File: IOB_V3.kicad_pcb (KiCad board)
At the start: 2 copper layers, 290 parts, among them J1 Conn_01x02, J10 Conn_01x04, J11 Conn_01x04, J12 Conn_01x04, J13 Conn_01x04, J14 Conn_01x04, J15 Conn_01x08, J16 Conn_02x04_Odd_Even, J17 Conn_01x04_MountingPin, J18 Conn_01x04_MountingPin, J19 Conn_01x04_MountingPin, J2 Conn_01x03, J20 Conn_01x04_MountingPin, J21 Conn_01x04_MountingPin, J22 Conn_01x04_MountingPin, J23 Conn_01x04_MountingPin, J24 Conn_01x04_MountingPin, J3 Conn_01x04, J4 Conn_01x04, J5 Conn_01x04, J6 Conn_01x04, J7 Conn_01x04, J8 Conn_01x04, J9 Conn_01x04, Q1 BSZ0902NSATMA1, Q10 BSZ0902NSATMA1, Q11 BSZ0902NSATMA1, Q12 BSZ0902NSATMA1, Q2 BSZ0902NSATMA1, Q3 BSZ0902NSATMA1, Q4 BSZ0902NSATMA1, Q5 BSZ0902NSATMA1, Q6 BSZ0902NSATMA1, Q7 BSZ0902NSATMA1, Q8 BSZ0902NSATMA1, Q9 BSZ0902NSATMA1, SW1 SW_Push_Dual, SW2 SW_Push_Dual, SW3 SW_DIP_x08, U1 REF3033, U10 INA180, U11 INA180, U12 INA180, U13 INA180, U14 TS30041, U15 MCP1700-3302E_SOT23, U16 MCP2562FD, U17 MCP2562FD, U18 STM32G474MET3, U19 W25Q256JV, U2 INA180, U3 INA180, U4 INA180, U5 INA180, U6 INA180, U7 INA180, U8 INA180, U9 INA180, X1 TXC-7C

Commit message: WIP
for @Markus
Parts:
- removed J20, J21, J22, J23, J24: Conn_01x04_MountingPin, Connector_JST:JST_GH_BM04B-GHS-TBT_1x04-1MP_P1.25mm_Vertical
- removed JP10, JP15, JP16, JP21, JP22, JP27, JP28, JP3, JP33, JP34, JP39, JP4, JP40, JP45, JP46, JP51, JP52, JP57, JP58, JP63, JP64, JP69, JP70, JP9: Jumper_2_Open, Jumper:SolderJumper-2_P1.3mm_Open_TrianglePad1.0x1.5mm
- removed R91: 120R, Resistor_SMD:R_0603_1608Metric
- added C23: 1u, Capacitor_SMD:C_0603_1608Metric, F.Cu at (137.5, 104.1)
- added R93: 0R, Resistor_SMD:R_0603_1608Metric, F.Cu at (134.5, 35.1)
- added R94: Rpullup, Resistor_SMD:R_0603_1608Metric, F.Cu at (134.5, 37.7)
- added TP2: TestPoint, TestPoint:TestPoint_THTPad_D1.0mm_Drill0.5mm, F.Cu at (138.0, 35.4)
- C11: value NP -> 100n; footprint Capacitor_SMD:CP_Elec_6.3x4.9 -> Capacitor_SMD:C_0402_1005Metric
- C12, C16, C17, C18: footprint Capacitor_SMD:C_0402_1005Metric -> Capacitor_SMD:C_0603_1608Metric
- C14: value 100n -> NP; footprint Capacitor_SMD:C_0402_1005Metric -> Capacitor_SMD:CP_Elec_6.3x4.9
- C19: value 100n -> 4.7u; footprint Capacitor_SMD:C_0402_1005Metric -> Capacitor_SMD:C_0603_1608Metric
- C20: value 100n -> 10n; footprint Capacitor_SMD:C_0402_1005Metric -> Capacitor_SMD:C_0603_1608Metric
- C21: value 10u -> 1u
- C22, C9: value 10u -> 100n
- C8: value 100n -> 10u; footprint Capacitor_SMD:C_0402_1005Metric -> Capacitor_SMD:C_0603_1608Metric
- J18: value Conn_01x04_MountingPin -> Conn_01x08; footprint Connector_JST:JST_GH_BM04B-GHS-TBT_1x04-1MP_P1.25mm_Vertical -> Connector_IDC:IDC-Header_2x04_P2.54mm_Horizontal
- U18: value STM32G474MET3 -> W25Q256JV; footprint STM32G747ME:STM32G474MET3 -> TXV_Library_Footprints:WSON-8-8x6mm
- U19: value W25Q256JV -> STM32G474MET6; footprint TXV_Library_Footprints:WSON-8-8x6mm -> STM32:STM32G474MET3
- moved J18 13.2 mm to (78.7, 33.3)
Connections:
- net /MCU/DIP_0 renamed Net-(SW3-Pad16)
- net /MCU/DIP_1 renamed Net-(SW3-Pad15)
- net /MCU/DIP_2 renamed Net-(SW3-Pad14)
- net /MCU/DIP_3 renamed Net-(SW3-Pad13)
- net /MCU/DIP_4 renamed Net-(SW3-Pad12)
- net /MCU/DIP_5 renamed Net-(SW3-Pad11)
- net /MCU/DIP_6 renamed Net-(SW3-Pad10)
- net /MCU/DIP_7 renamed Net-(SW3-Pad9)
- net /Pressure/Enable1 renamed /En1
- net /Pressure/Enable2 renamed /En2
- net /Pressure/Enable6 renamed /En6
- C13 pad 1: +3V3 -> GND
- C13 pad 2: GND -> +5V
- C17 pad 1: GND -> +3V3
- C17 pad 2: +5V -> GND
- C19 pad 1: GND -> +3V3
- C19 pad 2: +5V -> GND
- C20 pad 1: +3V3 -> /MCU/VDDA
- C21 pad 1: /MCU/VCAP1 -> /MCU/VDDA
- C22 pad 1: /MCU/VCAP2 -> +3.3VA
- C8 pad 1: +3V3 -> +5V
- C9 pad 1: +5V -> +3V3
- F12 pad 2: Net-(F12-Pad2) -> Net-(F11-Pad2)
- F14 pad 2: Net-(F14-Pad2) -> Net-(F13-Pad2)
- F16 pad 2: Net-(F16-Pad2) -> Net-(F15-Pad2)
- F18 pad 2: Net-(F18-Pad2) -> Net-(F17-Pad2)
- F2 pad 2: Net-(F2-Pad2) -> Net-(F1-Pad2)
- F20 pad 2: Net-(F20-Pad2) -> Net-(F19-Pad2)
- F22 pad 2: Net-(F22-Pad2) -> Net-(F21-Pad2)
- F24 pad 2: Net-(F24-Pad2) -> Net-(F23-Pad2)
- F4 pad 2: Net-(F4-Pad2) -> Net-(F3-Pad2)
- F6 pad 2: Net-(F6-Pad2) -> Net-(F5-Pad2)
- F8 pad 2: Net-(F8-Pad2) -> Net-(F7-Pad2)
- F9 pad 2: Net-(F9-Pad2) -> Net-(F10-Pad2)
- J10 pad 1: Net-(J10-Pad1) -> Net-(F15-Pad2)
- J11 pad 1: Net-(J11-Pad1) -> Net-(F17-Pad2)
- J12 pad 1: Net-(J12-Pad1) -> Net-(F19-Pad2)
- J13 pad 1: Net-(J13-Pad1) -> Net-(F21-Pad2)
- J14 pad 1: Net-(J14-Pad1) -> Net-(F23-Pad2)
- J18 pad 1: +5V -> unconnected-(J18-Pad1)
- J18 pad 2: /MCU/CANH2 -> unconnected-(J18-Pad2)
- J18 pad 3: /MCU/CANL2 -> unconnected-(J18-Pad3)
- J18 pad 4: GND -> unconnected-(J18-Pad4)
- J3 pad 1: Net-(J3-Pad1) -> Net-(F1-Pad2)
- J4 pad 1: Net-(J4-Pad1) -> Net-(F3-Pad2)
- J5 pad 1: Net-(J5-Pad1) -> Net-(F5-Pad2)
- J6 pad 1: Net-(J6-Pad1) -> Net-(F7-Pad2)
- J7 pad 1: Net-(J7-Pad1) -> Net-(F10-Pad2)
- J8 pad 1: Net-(J8-Pad1) -> Net-(F11-Pad2)
- J9 pad 1: Net-(J9-Pad1) -> Net-(F13-Pad2)
- JP11 pad 2: /Pressure/Select2 -> /Select2
- JP12 pad 1: /Pressure/Select2 -> /Select2
- JP17 pad 2: /Pressure/Select3 -> /Select3
- JP18 pad 1: /Pressure/Select3 -> /Select3
- JP23 pad 2: /Pressure/Select4 -> /Select4
- JP24 pad 1: /Pressure/Select4 -> /Select4
- JP29 pad 2: /Pressure/Select5 -> /Select5
- JP30 pad 1: /Pressure/Select5 -> /Select5
- JP35 pad 2: /Pressure/Select6 -> /Select6
- JP36 pad 1: /Pressure/Select6 -> /Select6
- JP41 pad 2: /Pressure/Select7 -> /Select7
- JP42 pad 1: /Pressure/Select7 -> /Select7
- JP47 pad 2: /Pressure/Select8 -> /Select8
- JP48 pad 1: /Pressure/Select8 -> /Select8
- JP5 pad 2: /Pressure/Select1 -> /Select1
- JP53 pad 2: /Pressure/Select9 -> /Select9
- JP54 pad 1: /Pressure/Select9 -> /Select9
- JP59 pad 2: /Pressure/Select10 -> /Select10
- JP6 pad 1: /Pressure/Select1 -> /Select1
- JP60 pad 1: /Pressure/Select10 -> /Select10
- JP65 pad 2: /Pressure/Select11 -> /Select11
- JP66 pad 1: /Pressure/Select11 -> /Select11
- JP71 pad 2: /Pressure/Select12 -> /Select12
- JP72 pad 1: /Pressure/Select12 -> /Select12
- R1 pad 2: /MCU/ADC1_INP10 -> /MCU/ADC1_IN1
- R15 pad 2: /MCU/ADC3_INP0 -> /MCU/ADC2_IN12
- R16 pad 1: /MCU/ADC3_INP0 -> /MCU/ADC2_IN12
- R18 pad 1: /Pressure/Enable3 -> /En3
- R2 pad 1: /MCU/ADC1_INP10 -> /MCU/ADC1_IN1
- R22 pad 2: /MCU/ADC3_INP1 -> /MCU/ADC1_IN5
- R23 pad 1: /MCU/ADC3_INP1 -> /MCU/ADC1_IN5
- R25 pad 1: /Pressure/Enable4 -> /En4
- R29 pad 2: /MCU/ADC1_INP4 -> /MCU/ADC1_IN4
- R30 pad 1: /MCU/ADC1_INP4 -> /MCU/ADC1_IN4
- R32 pad 1: /Pressure/Enable5 -> /En5
- R36 pad 2: /MCU/ADC1_INP8 -> /MCU/ADC1_IN8
- R37 pad 1: /MCU/ADC1_INP8 -> /MCU/ADC1_IN8
- R43 pad 2: /MCU/ADC1_INP16 -> /MCU/ADC2_IN5
- R44 pad 1: /MCU/ADC1_INP16 -> /MCU/ADC2_IN5
- R46 pad 1: /Pressure/Enable7 -> /En7
- R50 pad 2: /MCU/ADC1_INP17 -> /MCU/ADC2_IN11
- R51 pad 1: /MCU/ADC1_INP17 -> /MCU/ADC2_IN11
- R53 pad 1: /Pressure/Enable8 -> /En8
- R57 pad 2: /MCU/ADC1_INP14 -> /MCU/ADC1_IN14
- R58 pad 1: /MCU/ADC1_INP14 -> /MCU/ADC1_IN14
- R60 pad 1: /Pressure/Enable9 -> /En9
- R64 pad 2: /MCU/ADC1_INP15 -> /MCU/ADC2_IN3
- R65 pad 1: /MCU/ADC1_INP15 -> /MCU/ADC2_IN3
- R67 pad 1: /Pressure/Enable10 -> /En10
- R71 pad 2: /MCU/ADC1_INP18 -> /MCU/ADC3_IN7
- R72 pad 1: /MCU/ADC1_INP18 -> /MCU/ADC3_IN7
- R74 pad 1: /Pressure/Enable11 -> /En11
- R78 pad 2: /MCU/ADC1_INP19 -> /MCU/ADC3_IN4
- R79 pad 1: /MCU/ADC1_INP19 -> /MCU/ADC3_IN4
- R8 pad 2: /MCU/ADC1_INP11 -> /MCU/ADC1_IN2
- R81 pad 1: /Pressure/Enable12 -> /En12
- R9 pad 1: /MCU/ADC1_INP11 -> /MCU/ADC1_IN2
- U18 pad 1: unconnected-(U18-Pad1) -> /MCU/QUADSPI1_BK1_NCS
- U18 pad 2: unconnected-(U18-Pad2) -> /MCU/QUADSPI1_BK1_IO1
- U18 pad 3: unconnected-(U18-Pad3) -> /MCU/QUADSPI1_BK1_IO2
- U18 pad 4: unconnected-(U18-Pad4) -> GND
- U18 pad 5: unconnected-(U18-Pad5) -> /MCU/QUADSPI1_BK1_IO0
- U18 pad 6: unconnected-(U18-Pad6) -> /MCU/QUADSPI1_CLK
- U18 pad 7: unconnected-(U18-Pad7) -> /MCU/QUADSPI1_BK1_IO3
- U18 pad 8: unconnected-(U18-Pad8) -> +3V3
- U18 pad 9: unconnected-(U18-Pad9) -> (no net)
- U19 pad 1: /MCU/QUADSPI_BK1_NCS -> +3V3
- U19 pad 2: /MCU/QUADSPI_BK1_IO1 -> unconnected-(U19-Pad2)
- U19 pad 3: /MCU/QUADSPI_BK1_IO2 -> unconnected-(U19-Pad3)
- U19 pad 4: GND -> unconnected-(U19-Pad4)
- U19 pad 5: /MCU/QUADSPI_BK1_IO0 -> /MCU/CLK
- U19 pad 6: /MCU/QUADSPI_CLK -> unconnected-(U19-Pad6)
- U19 pad 7: /MCU/QUADSPI_BK1_IO3 -> /MCU/NRST
- U19 pad 8: +3V3 -> /Select6
- U19 pad 9: (no net) -> /En9

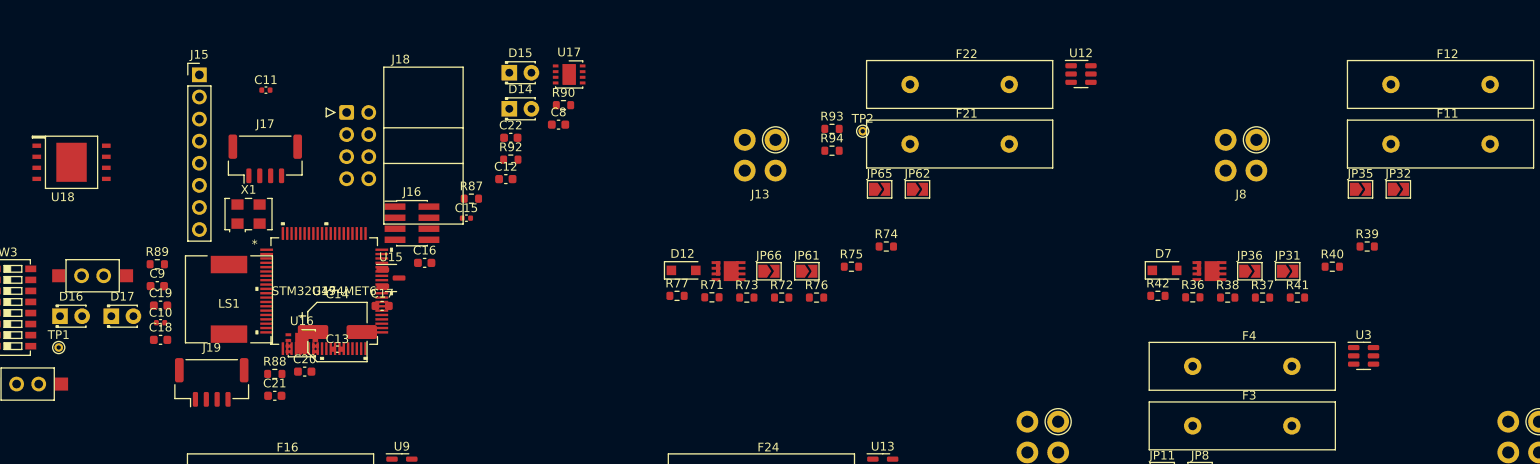
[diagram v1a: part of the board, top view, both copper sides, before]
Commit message: Schematic nearly complete
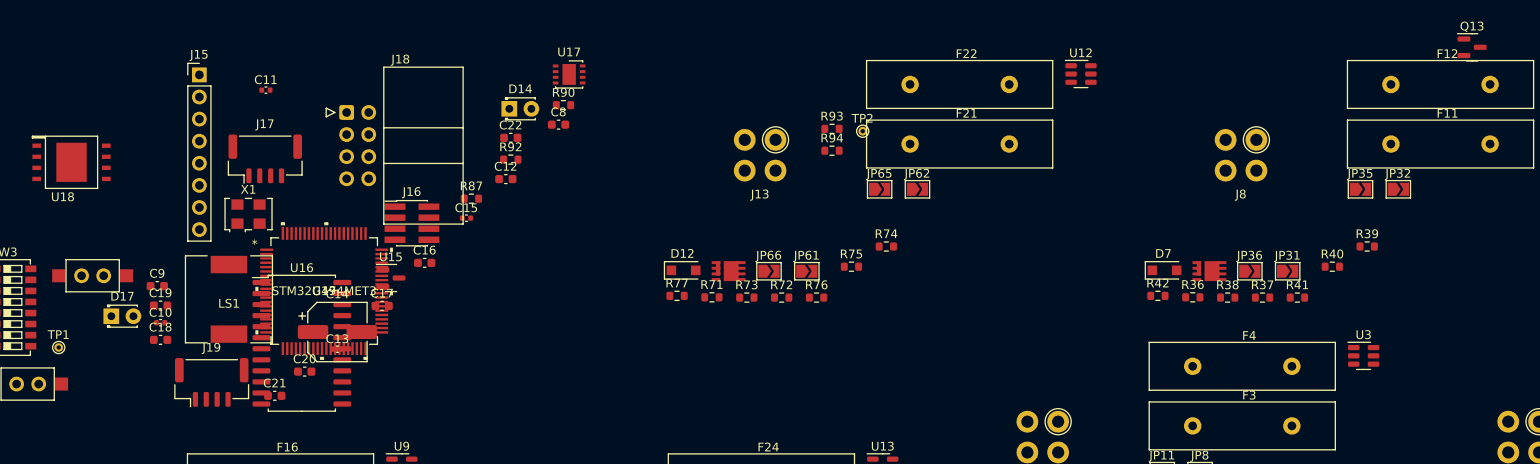
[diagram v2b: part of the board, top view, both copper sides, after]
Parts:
- removed D15, D16: LED, LED_THT:LED_D1.8mm_W3.3mm_H2.4mm
- removed R88, R89: 120R, Resistor_SMD:R_0603_1608Metric
- added Q13: SI2300, Package_TO_SOT_SMD:SOT-23, F.Cu at (208.0, 25.8)
- U16: value MCP2562FD -> CD74HC4067M; footprint Package_DFN_QFN:DFN-8-1EP_3x3mm_P0.65mm_EP1.55x2.4mm -> Package_SO:SOIC-24W_7.5x15.4mm_P1.27mm
- U19: value STM32G474MET6 -> STM32G474MET3
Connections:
- J18 pad 1: unconnected-(J18-Pad1) -> /MCU/SPI4_SCK
- J18 pad 2: unconnected-(J18-Pad2) -> /MCU/SPI4_MOSI
- J18 pad 3: unconnected-(J18-Pad3) -> /MCU/SPI4_MISO
- J18 pad 4: unconnected-(J18-Pad4) -> /MCU/SPI4_NSS1
- J18 pad 5: unconnected-(J18-Pad5) -> /MCU/SPI4_NSS2
- J18 pad 6: unconnected-(J18-Pad6) -> /MCU/SPI4_NSS3
- J18 pad 7: unconnected-(J18-Pad7) -> /MCU/SPI4_NSS4
- LS1 pad 1: /MCU/Speaker_1 -> +3V3
- LS1 pad 2: /MCU/Speaker_2 -> Net-(LS1-Pad2)
- U16 pad 1: /MCU/CAN2_TX -> /MCU/SPI4_NSS
- U16 pad 2: GND -> unconnected-(U16-Pad2)
- U16 pad 3: +5V -> unconnected-(U16-Pad3)
- U16 pad 4: /MCU/CAN2_RX -> unconnected-(U16-Pad4)
- U16 pad 5: +3V3 -> unconnected-(U16-Pad5)
- U16 pad 6: /MCU/CANL2 -> /MCU/SPI4_NSS4
- U16 pad 7: /MCU/CANH2 -> /MCU/SPI4_NSS3
- U16 pad 8: GND -> /MCU/SPI4_NSS2
- U16 pad 9: GND -> /MCU/SPI4_NSS1

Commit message: Routing begin
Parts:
- removed C20: 10n, Capacitor_SMD:C_0603_1608Metric
- removed C21, C23: 1u, Capacitor_SMD:C_0603_1608Metric
- removed C22: 100n, Capacitor_SMD:C_0603_1608Metric
- added D15: LED, LED_THT:LED_D1.8mm_W3.3mm_H2.4mm, F.Cu at (125.3, 21.0)
- added D16: LED, LED_THT:LED_D1.8mm_W3.3mm_H2.4mm, F.Cu at (125.3, 25.6)
- added R88: 120R, Resistor_SMD:R_0603_1608Metric, F.Cu at (132.1, 21.0)
- added R89: 120R, Resistor_SMD:R_0603_1608Metric, F.Cu at (132.0, 25.5)
- added U20: CD74HC4067M, Package_SO:SOIC-24W_7.5x15.4mm_P1.27mm, F.Cu at (179.5, 74.8)
- F1, F10, F11, F12, F13, F14, F15, F16, F17, F18, F19, F2, F20, F21, F22, F23, F24, F25, F3, F4, F5, F6, F7, F8, F9: footprint Fuse:Fuse_Littelfuse-LVR125 -> TXV_Library_Footprints:0805L110SL PPTC Polyfuse Littelfuse
- moved C19 184.0 mm to (238.6, 23.8)
- moved C18 182.9 mm to (237.9, 30.7)
- moved C9 174.8 mm to (229.1, 23.4)
- moved TP1 166.4 mm to (207.7, 23.1)
- moved F23 161.9 mm to (280.5, 56.6)
- moved JP67 161.9 mm to (268.6, 71.2)
- moved JP71 161.9 mm to (277.0, 61.8)
- moved R83 161.9 mm to (269.7, 74.3)
- moved J14 161.9 mm to (263.2, 57.9)
- moved R81 161.9 mm to (277.7, 68.4)
- moved R82 161.9 mm to (273.7, 70.7)
- moved R84 161.9 mm to (253.7, 74.1)
- moved D13 161.9 mm to (254.4, 71.1)
- moved JP68 161.9 mm to (281.3, 61.8)
- moved JP72 161.9 mm to (264.3, 71.2)
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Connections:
- U16 pad 10: /MCU/MUX_SEL0 -> /MCU/MUX1_SEL0
- U16 pad 11: /MCU/MUX_SEL1 -> /MCU/MUX1_SEL1
- U16 pad 13: /MCU/MUX_SEL3 -> /MCU/MUX1_SEL3
- U16 pad 14: /MCU/MUX_SEL2 -> /MCU/MUX1_SEL2
- U16 pad 15: /MCU/MUX_~{EN} -> /MCU/MUX1_~{EN}
- U19 pad 19: /Select7 -> /MCU/INPUT_SELECT
- U19 pad 29: /MCU/VDDA -> +3.3VA
- U19 pad 31: unconnected-(U19-Pad31) -> /MCU/MUX1_SEL2
- U19 pad 32: unconnected-(U19-Pad32) -> /MCU/MUX1_SEL3
- U19 pad 33: unconnected-(U19-Pad33) -> /MCU/MUX1_~{EN}
- U19 pad 43: /MCU/SPI2_NSS -> /MCU/STATUS_LED_1
- U19 pad 44: /Select12 -> /MCU/STATUS_LED_2
- U19 pad 46: /Select9 -> /MCU/DEBUG_LED
- U19 pad 47: unconnected-(U19-Pad47) -> /MCU/MUX1_SEL0
- U19 pad 48: unconnected-(U19-Pad48) -> /MCU/MUX1_SEL1
- U19 pad 53: /Select11 -> /MCU/BUTTON_1
- U19 pad 56: /Select8 -> /MCU/MUX2_SEL0
- U19 pad 57: /Select1 -> /MCU/MUX2_SEL1
- U19 pad 58: /Select5 -> /MCU/MUX2_SEL2
- U19 pad 60: /Select10 -> /MCU/MUX2_SEL3
- U19 pad 68: unconnected-(U19-Pad68) -> /OneWire
- U19 pad 69: unconnected-(U19-Pad69) -> /En6
- U19 pad 70: unconnected-(U19-Pad70) -> /En1
- U19 pad 71: unconnected-(U19-Pad71) -> /En2
- U19 pad 72: /Select2 -> /MCU/Speaker_1
- U19 pad 74: /Select4 -> unconnected-(U19-Pad74)
- U19 pad 78: /Select3 -> /MCU/MUX2_~{EN}
- U19 pad 8: /Select6 -> unconnected-(U19-Pad8)

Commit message: Routing WIP
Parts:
- moved R93 110.9 mm to (130.5, 64.8)
- moved R94 110.9 mm to (130.3, 68.6)
- moved TP2 110.7 mm to (134.3, 68.6)
- moved C19 92.9 mm to (155.0, 64.6)
- moved C18 90.1 mm to (155.0, 66.1)
- moved C9 88.8 mm to (155.0, 72.3)
- moved C12 86.4 mm to (155.0, 70.8)
- moved C17 86.4 mm to (155.0, 67.7)
- moved C16 84.1 mm to (155.0, 69.2)
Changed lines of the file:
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@@
   )
   (footprint "Capacitor_SMD:C_0603_1608Metric" (layer "F.Cu")
-    (at 237.9 30.67)
+    (at 155.025 66.125)
     (descr "Capacitor SMD 0603 (1608 Metric), square (rectangular) end terminal, IPC_7351 nominal, (Body size source: IPC-SM-782 page 76, https://www.pcb-3d.com/wordpress/wp-content/uploads/ipc-sm-782a_amendment_1_and_2.pdf), generated with kicad-footprint-generator")
     (tags "capacitor")
@@
     (property "Sheetname" "MCU")
     (attr smd)
-    (fp_text reference "C18" (at 0 -1.43) (layer "F.SilkS")
+    (fp_text reference "C18" (at 0 -1.43) (layer "F.SilkS") hide
       (effects (font (size 1 1) (thickness 0.15)))
     )
@@
   )
   (footprint "Resistor_SMD:R_0603_1608Metric" (layer "F.Cu")
-    (at 233.515 23.655)
+    (at 130.475 64.77)
     (descr "Resistor SMD 0603 (1608 Metric), square (rectangular) end terminal, IPC_7351 nominal, (Body size source: IPC-SM-782 page 72, https://www.pcb-3d.com/wordpress/wp-content/uploads/ipc-sm-782a_amendment_1_and_2.pdf), generated with kicad-footprint-generator")
     (tags "resistor")
@@
   )
   (footprint "Capacitor_SMD:C_0603_1608Metric" (layer "F.Cu")
-    (at 233.26 31.1)
+    (at 155.025 67.675)
     (descr "Capacitor SMD 0603 (1608 Metric), square (rectangular) end terminal, IPC_7351 nominal, (Body size source: IPC-SM-782 page 76, https://www.pcb-3d.com/wordpress/wp-content/uploads/ipc-sm-782a_amendment_1_and_2.pdf), generated with kicad-footprint-generator")
     (tags "capacitor")
@@
     (property "Sheetname" "MCU")
     (attr smd)
-    (fp_text reference "C17" (at 0 -1.43) (layer "F.SilkS")
+    (fp_text reference "C17" (at 0 -1.43) (layer "F.SilkS") hide
       (effects (font (size 1 1) (thickness 0.15)))
     )
@@
   )
   (footprint "Capacitor_SMD:C_0603_1608Metric" (layer "F.Cu")
-    (at 229.11 23.44)
+    (at 155.025 72.325)
     (descr "Capacitor SMD 0603 (1608 Metric), square (rectangular) end terminal, IPC_7351 nominal, (Body size source: IPC-SM-782 page 76, https://www.pcb-3d.com/wordpress/wp-content/uploads/ipc-sm-782a_amendment_1_and_2.pdf), generated with kicad-footprint-generator")
     (tags "capacitor")
@@
     (property "Sheetname" "MCU")
     (attr smd)
-    (fp_text reference "C9" (at 0 -1.43) (layer "F.SilkS")
+    (fp_text reference "C9" (at 0 -1.43) (layer "F.SilkS") hide
       (effects (font (size 1 1) (thickness 0.15)))
     )
@@
   )
   (footprint "Capacitor_SMD:C_0603_1608Metric" (layer "F.Cu")
-    (at 229.07 29.34)
+    (at 155.025 69.225)
     (descr "Capacitor SMD 0603 (1608 Metric), square (rectangular) end terminal, IPC_7351 nominal, (Body size source: IPC-SM-782 page 76, https://www.pcb-3d.com/wordpress/wp-content/uploads/ipc-sm-782a_amendment_1_and_2.pdf), generated with kicad-footprint-generator")
     (tags "capacitor")
@@
     (property "Sheetname" "MCU")
     (attr smd)
-    (fp_text reference "C16" (at 0 -1.43) (layer "F.SilkS")
+    (fp_text reference "C16" (at 0 -1.43) (layer "F.SilkS") hide
       (effects (font (size 1 1) (thickness 0.15)))
     )
@@
   )
   (footprint "TestPoint:TestPoint_THTPad_D1.0mm_Drill0.5mm" (layer "F.Cu")
-    (at 236.98 27.3)
+    (at 134.3 68.625)
     (descr "THT pad as test Point, diameter 1.0mm, hole diameter 0.5mm")
     (tags "test point THT pad")
@@
   )
   (footprint "Capacitor_SMD:C_0603_1608Metric" (layer "F.Cu")
-    (at 238.55 23.8)
+    (at 155.025 64.575)
     (descr "Capacitor SMD 0603 (1608 Metric), square (rectangular) end terminal, IPC_7351 nominal, (Body size source: IPC-SM-782 page 76, https://www.pcb-3d.com/wordpress/wp-content/uploads/ipc-sm-782a_amendment_1_and_2.pdf), generated with kicad-footprint-generator")
     (tags "capacitor")
@@
     (property "Sheetname" "MCU")
     (attr smd)
-    (fp_text reference "C19" (at 0 -1.43) (layer "F.SilkS")
+    (fp_text reference "C19" (at 0 -1.43) (layer "F.SilkS") hide
       (effects (font (size 1 1) (thickness 0.15)))
     )
@@
   )
   (footprint "Resistor_SMD:R_0603_1608Metric" (layer "F.Cu")
-    (at 233.34 27.46)
+    (at 130.3 68.575)
     (descr "Resistor SMD 0603 (1608 Metric), square (rectangular) end terminal, IPC_7351 nominal, (Body size source: IPC-SM-782 page 72, https://www.pcb-3d.com/wordpress/wp-content/uploads/ipc-sm-782a_amendment_1_and_2.pdf), generated with kicad-footprint-generator")
     (tags "resistor")
@@
   )
   (footprint "Capacitor_SMD:C_0603_1608Metric" (layer "F.Cu")
-    (at 229.23 26.52)
+    (at 155.025 70.775)
     (descr "Capacitor SMD 0603 (1608 Metric), square (rectangular) end terminal, IPC_7351 nominal, (Body size source: IPC-SM-782 page 76, https://www.pcb-3d.com/wordpress/wp-content/uploads/ipc-sm-782a_amendment_1_and_2.pdf), generated with kicad-footprint-generator")
     (tags "capacitor")
@@
     (property "Sheetname" "MCU")
     (attr smd)
-    (fp_text reference "C12" (at 0 -1.43) (layer "F.SilkS")
+    (fp_text reference "C12" (at 0 -1.43) (layer "F.SilkS") hide
       (effects (font (size 1 1) (thickness 0.15)))
     )
@@
     )
   )
-  (group "" (id 7e70563d-20b1-47b7-ae21-9de68c3388f1)
-    (members
-      10eda7e0-58cb-4103-9491-731ead664fb6
-      300aa512-2f66-4c26-a530-50c091b3a099
-      37e25b07-cf59-45fe-844f-5417bc730cd4
-      4c2fb79c-207e-4f92-8ea1-7543e9ed400d
-      4ef92708-c2d9-4531-af23-a1f9f476bf8c
-      71e41a10-44db-4346-b6f4-dfa3ed0bff8e
-      82a6fa17-8830-478d-9595-5eea2fe7cc7f
-      8c76b6f5-ee3a-4ad1-bdeb-0ae5ad222b2c
-      9141dbb7-513a-4a00-a5a5-e91c4c8d872d
-      a7f9e962-df3d-48ec-bb65-e4cd721b1fdb
-      a951150c-9089-41ba-8bfe-69460782c403
-      aff00d57-63ea-46b6-99f8-32eff51e9707
-      e454861c-dc15-4164-baf5-32394e274b30
-      e4957fbd-8bef-42d4-bb57-1c907e00bc66
-      e6c16de8-82c4-4dbf-98f0-9455be9a104c
-      f0412283-6407-4174-b91b-30d83aae4df4
-    )
-  )

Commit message: Connection layout set
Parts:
- moved JP62 82.7 mm to (199.3, 38.3), turned to 90 degrees
- moved R75 78.5 mm to (196.0, 37.4)
- moved F21 77.3 mm to (203.8, 27.5), turned to 90 degrees
- moved U18 77.2 mm to (136.8, 96.3)
- moved JP61 74.2 mm to (196.1, 30.8)
- moved R74 72.2 mm to (206.5, 33.3), turned to 180 degrees
- moved R72 71.3 mm to (196.0, 34.4), turned to 180 degrees
- moved JP65 71.2 mm to (206.5, 29.6), turned to 180 degrees
- moved F22 68.7 mm to (201.8, 27.5), turned to 90 degrees
- moved R73 67.1 mm to (196.0, 35.9), turned to 180 degrees
- moved R76 65.5 mm to (206.5, 31.7), turned to 180 degrees
- moved R71 63.7 mm to (196.0, 32.9)
- moved J13 62.7 mm to (201.2, 33.0)
- moved JP66 60.6 mm to (206.5, 27.1), turned to 180 degrees
- moved U12 58.6 mm to (198.6, 26.8)
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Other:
- copper layers 2 -> 4
- board text added: "#"
- board text added: "*"
- board text added: "4-20mA d/a Input d Output"
- board text added: "Ch1"
- board text added: "Ch10"
- board text added: "Ch11"
- board text added: "Ch12"
- board text added: "Ch2"
- board text added: "Ch3"
- board text added: "Ch4"
- board text added: "Ch5"
- board text added: "Ch6"
- board text added: "Ch7"
- board text added: "Ch8"
- board text added: "Ch9"
- board text added: "o"
- board text added: "~"

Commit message: Layout WIP
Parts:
- D14, D15, D16, D17: footprint LED_THT:LED_D1.8mm_W3.3mm_H2.4mm -> LED_SMD:LED_0603_1608Metric
- J18: footprint Connector_IDC:IDC-Header_2x04_P2.54mm_Horizontal -> Connector_IDC:IDC-Header_2x04_P2.54mm_Vertical
- moved D5 189.8 mm to (215.9, 70.3)
- moved F7 189.8 mm to (212.5, 59.5)
- moved F8 189.8 mm to (210.5, 59.5)
- moved J6 189.8 mm to (210.0, 65.0)
- moved JP19 189.8 mm to (204.8, 62.8)
- moved JP20 189.8 mm to (208.0, 70.3)
- moved JP23 189.8 mm to (215.2, 61.6)
- moved JP24 189.8 mm to (215.2, 59.1)
- moved Q4 189.8 mm to (211.8, 70.5)
- moved R22 189.8 mm to (204.7, 64.9)
- moved R23 189.8 mm to (204.7, 66.4)
- moved R24 189.8 mm to (204.7, 67.9)
- moved R25 189.8 mm to (215.2, 65.3)
- moved R26 189.8 mm to (204.7, 69.4)
- moved R27 189.8 mm to (215.2, 63.7)
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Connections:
- SW3 pad 10: Net-(SW3-Pad10) -> /MCU/GND2
- SW3 pad 11: Net-(SW3-Pad11) -> /MCU/GND3
- SW3 pad 12: Net-(SW3-Pad12) -> /MCU/GND4
- SW3 pad 13: Net-(SW3-Pad13) -> /MCU/GND5
- SW3 pad 14: Net-(SW3-Pad14) -> /MCU/GND6
- SW3 pad 15: Net-(SW3-Pad15) -> /MCU/GND7
- SW3 pad 16: Net-(SW3-Pad16) -> /MCU/GND8
- SW3 pad 9: Net-(SW3-Pad9) -> /MCU/GND1
- U16 pad 16: Net-(SW3-Pad9) -> /MCU/GND8
- U16 pad 17: Net-(SW3-Pad10) -> /MCU/GND7
- U16 pad 18: Net-(SW3-Pad11) -> /MCU/GND6
- U16 pad 19: Net-(SW3-Pad12) -> /MCU/GND5
- U16 pad 20: Net-(SW3-Pad13) -> /MCU/GND4
- U16 pad 21: Net-(SW3-Pad14) -> /MCU/GND3
- U16 pad 22: Net-(SW3-Pad15) -> /MCU/GND2
- U16 pad 23: Net-(SW3-Pad16) -> /MCU/GND1
- U19 pad 19: /MCU/INPUT_SELECT -> /MCU/DEBUG_LED
- U19 pad 46: /MCU/DEBUG_LED -> /MCU/INPUT_SELECT
- U19 pad 72: /MCU/Speaker_1 -> /MCU/MUX2_~{EN}
- U19 pad 78: /MCU/MUX2_~{EN} -> /MCU/Speaker_1
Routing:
- added copper zone on F.Cu, net +3V3
- added copper zone on B.Cu, net GND
- added copper zone on F.Cu, net GND
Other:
- board outline added: 140 x 80 mm
- board text added: "5V Supply"
